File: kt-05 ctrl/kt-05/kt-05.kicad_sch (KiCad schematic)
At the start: 14 parts, among them CN1 PJ-332A-6A, CN2 PJ-332A-6A, CN3 Pogo Pin Receptor Right, U1 SLSS49E-3, U2 SLSS49E-3, U6 H11L1S(TA), U7 Pogo Pin Left, U8 AP2112K-3.3

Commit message: core mainboard
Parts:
- removed CN1, CN2: PJ-332A-6A, easyeda2kicad:AUDIO-SMD_PJ-332A-6A, symbol easyeda2kicad:PJ-332A-6A
- removed U1, U2: SLSS49E-3, samparts:SLSS49E_Hall_Switch_MX, symbol easyeda2kicad:SLSS49E-3
- removed U8: AP2112K-3.3, Package_TO_SOT_SMD:SOT-23-5, symbol Regulator_Linear:AP2112K-3.3
- added C1, C2, C4: 10u, Capacitor_SMD:C_0402_1005Metric, symbol Device:C
- added C3: 0.1u, Capacitor_SMD:C_0402_1005Metric, symbol Device:C
- added C5, C6: 1u, Capacitor_SMD:C_0402_1005Metric, symbol Device:C
- added CN10, CN11, CN12, CN13, CN14, CN3, CN5, CN6, CN7, CN8, CN9: YTC1P-6030-01, easyeda2kicad:SMD-1_BD2.0-H10.0, symbol easyeda2kicad:YTC1P-6030-01
- added CN15: MIDI IN, easyeda2kicad:AUDIO-SMD_PJ-327A5JJ, symbol easyeda2kicad:PJ-327A5JJ
- added CN16: MIDI OUT, easyeda2kicad:AUDIO-SMD_PJ-327A5JJ, symbol easyeda2kicad:PJ-327A5JJ
- added D2: SS34_C8678, easyeda2kicad:SMA_L4.3-W2.6-LS5.2-RD, symbol easyeda2kicad:SS34_C8678
- added D3: 1N4148W, Diode_SMD:D_SOD-123, symbol Diode:1N4148W
- added FPC1: 0.5K-A-8PB, easyeda2kicad:FPC-SMD_8P-P0.50_HDGC_0.5K-A-8PB, symbol easyeda2kicad:0.5K-A-8PB
- added H2: WAFER-PH2.0-2PWB, easyeda2kicad:CONN-SMD_2P-P2.00_XUNPU_WAFER-PH2.0-2PWB, symbol easyeda2kicad:WAFER-PH2.0-2PWB
- added H3: MountingHole_Pad, MountingHole:MountingHole_2.7mm_M2.5_DIN965_Pad_TopBottom, symbol Mechanical:MountingHole_Pad
- added J1: Conn_01x06, Connector_PinHeader_2.54mm:PinHeader_1x06_P2.54mm_Vertical, symbol Connector_Generic:Conn_01x06
- added Q1, Q2, Q3: AO3401A, Package_TO_SOT_SMD:SOT-23, symbol Transistor_FET:AO3401A
- added R2, R24, R6, R7, R8, R9: 10K, Resistor_SMD:R_0402_1005Metric, symbol Device:R
- added R20: 5.1k, Resistor_SMD:R_0402_1005Metric, symbol Device:R
- added R21, R22, R23: 100K, Resistor_SMD:R_0402_1005Metric, symbol Device:R
- added R25: 1M, Resistor_SMD:R_0402_1005Metric, symbol Device:R
- added R26: 10, Resistor_SMD:R_0402_1005Metric, symbol Device:R
- added R27: 33, Resistor_SMD:R_0402_1005Metric, symbol Device:R
- added R28, R29: 470, Resistor_SMD:R_0402_1005Metric, symbol Device:R
- added R5: 22R, Resistor_SMD:R_0402_1005Metric, symbol Device:R
- added SW1: ESP RST, easyeda2kicad:SW-SMD_L3.9-W3.0-P4.45, symbol easyeda2kicad:TS-1088-AR02016
- added SW2: ESP BOOT, easyeda2kicad:SW-SMD_L3.9-W3.0-P4.45, symbol easyeda2kicad:TS-1088-AR02016
- added U1: SK6812MINI-HS, easyeda2kicad:LED-SMD_4P-L3.5-W3.5-BR_SK6812MINI-HS, symbol easyeda2kicad:SK6812MINI-HS
- added U10, U11, U12, U13, U14, U15, U16, U17, U18, U19, U20, U21, U22, U23, U7: H3V3U10B, easyeda2kicad:DFN1006-2L-BI, symbol easyeda2kicad:H3V3U10B
- added U2: AP2112K-3.3, Package_TO_SOT_SMD:SOT-23-5, symbol Regulator_Linear:AP2112K-3.3
- added U3: MCP73831-2-OT, Package_TO_SOT_SMD:SOT-23-5, symbol Battery_Management:MCP73831-2-OT
- added U4: PS-5850SVB-6PL, easyeda2kicad:SW-SMD_6P-L5.8-W5.8-P2.00-LS11.3, symbol easyeda2kicad:PS-5850SVB-6PL
- added U6: ATtiny1616-M, Package_DFN_QFN:VQFN-20-1EP_3x3mm_P0.4mm_EP1.7x1.7mm, symbol MCU_Microchip_ATtiny:ATtiny1616-M
- added U8: ESP32-S3-MINI-1, RF_Module:ESP32-S2-MINI-1, symbol RF_Module:ESP32-S3-MINI-1
- renumbered CN3 to CN4, D2 to D1, F2 to F1, R5 to R3, U6 to U5, U7 to U9
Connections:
- net +3.3V: now also R4.1, U5.6 (VCC), C2.1, C3.1, FPC1.7, J1.2 (Pin_2), R24.1, R27.1, R28.2, R5.2, R6.1, R7.1, R8.1, R9.1, U1.3 (VDD), U2.5 (VOUT), U6.4 (VCC), U8.3 (3V3)
- net +5V: now also R2.2, R20.1, U3.4 (V_{DD}), U4.3
- net DN: now also U8.23 (USB_D-)
- net DP: now also U8.24 (USB_D+)
- net GND: now also U5.5 (GND), C1.2, C2.2, C3.2, C4.2, C5.2, C6.2, CN16.1, CN16.2, FPC1.10, FPC1.2, FPC1.9, H2.2, H2.3, H2.4, J1.1 (Pin_1), R21.2, R25.2, SW1.2, SW2.2, U1.1 (GND), U10.2, U11.2, U12.2, U13.2, U14.1, U15.1, U16.1, U17.1, U18.1, U19.1, U2.2 (GND), U20.1, U21.1, U22.1, U23.1, U3.2 (V_{SS}), U6.21 (GND), U6.3 (GND), U7.1, U8.1 (GND), U8.2 (GND), U8.42 (GND), U8.43 (GND), U8.46 (GND), U8.47 (GND), U8.48 (GND), U8.49 (GND), U8.50 (GND), U8.51 (GND), U8.52 (GND), U8.53 (GND), U8.54 (GND), U8.55 (GND), U8.56 (GND), U8.57 (GND), U8.58 (GND), U8.59 (GND), U8.60 (GND), U8.61 (GND), U8.62 (GND), U8.63 (GND), U8.64 (GND), U8.65 (GND)
- net SCL0: now also J1.5 (Pin_5), R6.2, U11.1, U6.14 (PB0), U8.5 (IO1)
- net SCL1: now also R8.2, U13.1, U8.38 (IO42)
- net SDA0: now also J1.4 (Pin_4), R7.2, U10.1, U6.13 (PB1), U8.6 (IO2)
- net SDA1: now also R9.2, U12.1, U8.37 (IO41)
- net at U5.1 (AN): now also D3.1 (K), R29.1
- net at U5.2 (CAT): now also CN15.4, D3.2 (A)
- net ESP_RXD0: now reaches U5.4 (VO)
- net ESP_RXD0: now also R28.1, U8.40 (RXD0)
- removed net VBUS: CN4.3, R4.2, U9.2
- new net: CN16.4, R26.2
- new net: D2.2 (A), Q3.1 (G), R21.1, U4.2
- new net: FPC1.1, R5.1
- new net: R20.2, U3.5 (PROG)
- new net: CN15.3, R29.2
- new net: R2.1, U2.3 (EN)
- new net: CN16.3, R27.2
- new net A0: CN6.1, U15.2, U6.5 (PA4)
- new net A1: CN14.1, U23.2, U6.6 (PA5)
- new net A14: CN9.1, U18.2, U6.20 (PA1)
- new net A15: CN8.1, U17.2, U6.1 (PA2)
- new net A16: CN7.1, U16.2, U6.2 (PA3)
- new net A2: CN13.1, U22.2, U6.7 (PA6)
- new net A3: CN12.1, U21.2, U6.8 (PA7)
- new net A4: U6.9 (PB5)
- new net CG_STAT: U3.1 (STAT), U8.36 (IO40)
- new net D10: CN3.1, U6.15 (PC0), U7.2
- new net D11: CN5.1, U14.2, U6.16 (PC1)
- new net D12: CN11.1, U20.2, U6.17 (PC2)
- new net D13: CN10.1, U19.2, U6.18 (PC3)
- new net DBLTAP: C6.1, R25.1, U8.29 (IO34)
- new net ESP_BOOT: SW2.1, U8.4 (IO0)
- new net ESP_RST: C5.1, R24.2, SW1.1, U8.45 (EN)
- new net ESP_TXD0: R26.1, U8.39 (TXD0)
- new net NEO: U1.2 (DIN), U8.15 (IO11)
- new net TFT_CS: FPC1.8, U8.22 (IO18)
- new net TFT_DC: FPC1.4, U8.19 (IO15)
- new net TFT_MOSI: FPC1.5, U8.20 (IO16)
- new net TFT_RST: FPC1.3, U8.18 (IO14)
- new net TFT_SCK: FPC1.6, U8.21 (IO17)
- new net TXD: J1.6 (Pin_6), U6.12 (PB2)
- new net UPDI: J1.3 (Pin_3), R4.2, U6.19 (~{RESET}/PA0)
- new net VBAT: C4.1, H2.1, Q3.3 (D), U3.3 (V_{BAT})
- new net VHIGH: C1.1, D2.1 (K), Q1.2 (S), Q2.2 (S), Q3.2 (S), R22.1, R23.1, U2.1 (VIN)
- new net VLEFT: Q1.3 (D), U9.2
- new net VLEFTCTL: Q1.1 (G), R23.2, U8.7 (IO3)
- new net VRIGHT: CN4.3, Q2.3 (D)
- new net VRIGHTCTL: Q2.1 (G), R22.2, U8.35 (IO39)
- no-connect marks 2 -> 15
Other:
- note added: "1.14in screen https://www.buydisplay.com/1-14-inch-tft-lcd-display-ips-panel-screen-135x240-for-smart-watch"
- note added: "Battery 420mAh https://www.pkcell.com/product/lp552535-420mah-3-7v/"
- note added: "UPDI/debug header"
- moved on the sheet: CN4, D1, F1, R1, R3, U5, U9, USBC1

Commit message: ch
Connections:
- net GND: now also CN4.1, U9.4; no longer CN4.4, U9.1
- net SCL0: now also U9.1; no longer U9.4
- net SCL1: now also CN4.4; no longer CN4.1
- net SDA0: now also U9.2; no longer U9.3
- net SDA1: now also CN4.3; no longer CN4.2
- net VLEFT: now also U9.3; no longer U9.2
- net VRIGHT: now also CN4.2; no longer CN4.3
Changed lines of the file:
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@@
 		(lib_id "easyeda2kicad:YZ165615055F-04025-01")
 		(at 532.13 102.87 0)
+		(mirror x)
 		(unit 1)
 		(exclude_from_sim no)
@@
 		(on_board yes)
 		(dnp no)
-		(fields_autoplaced yes)
 		(property "Reference" "U9"
-			(at 535.94 101.5999 0)
+			(at 535.94 104.1401 0)
 			(effects
 				(font
@@
 		)
 		(property "Value" "Pogo Pin Left"
-			(at 535.94 104.1399 0)
+			(at 535.94 101.6001 0)
 			(effects
 				(font
@@
 		)
 		(property "Footprint" "easyeda2kicad:CONN-SMD_4P-L11.0-W5.5-P2.50_YZ165615055F-04025-01"
-			(at 532.13 114.3 0)
+			(at 532.13 91.44 0)
 			(effects
 				(font
@@
 		)
 		(property "LCSC Part" "C5296819"
-			(at 532.13 116.84 0)
+			(at 532.13 88.9 0)
 			(effects
 				(font
@@
 		(lib_id "easyeda2kicad:YZ199315035T-04025-01")
 		(at 532.13 116.84 0)
+		(mirror x)
 		(unit 1)
 		(exclude_from_sim no)
@@
 		(on_board yes)
 		(dnp no)
-		(fields_autoplaced yes)
 		(property "Reference" "CN4"
-			(at 535.94 115.5699 0)
+			(at 535.94 118.1101 0)
 			(effects
 				(font
@@
 		)
 		(property "Value" "Pogo Pin Receptor Right"
-			(at 535.94 118.1099 0)
+			(at 535.94 115.5701 0)
 			(effects
 				(font
@@
 		)
 		(property "Footprint" "easyeda2kicad:CONN-SMD_YZ199315035T-04025-01"
-			(at 532.13 128.27 0)
+			(at 532.13 105.41 0)
 			(effects
 				(font
@@
 		)
 		(property "LCSC Part" "C5296825"
-			(at 532.13 130.81 0)
+			(at 532.13 102.87 0)
 			(effects
 				(font

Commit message: many
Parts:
- added R10, R11: 10K, Resistor_SMD:R_0402_1005Metric, symbol Device:R
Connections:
- net GND: now also R10.2
- net VBAT: now also R11.1
- net BAT_DET: now reaches U8.17 (IO13)
- net BAT_DET: now also R10.1, R11.2

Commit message: prod
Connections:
- net A14: now also U6.14 (PB0); no longer U6.20 (PA1)
- net A15: now also U6.13 (PB1); no longer U6.1 (PA2)
- net A16: now also U6.10 (PB4); no longer U6.2 (PA3)
- net SCL0: now also U6.1 (PA2); no longer U6.14 (PB0)
- net SDA0: now also U6.20 (PA1); no longer U6.13 (PB1)
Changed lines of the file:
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@@
 	)
 	(no_connect
+		(at 215.9 38.1)
+	)
+	(no_connect
 		(at 43.18 175.26)
 	)
@@
 	)
 	(no_connect
-		(at 215.9 63.5)
-	)
-	(no_connect
 		(at 92.71 60.96)
 	)
@@
 	(wire
 		(pts
-			(xy 218.44 33.02) (xy 215.9 33.02)
+			(xy 215.9 33.02) (xy 220.98 33.02)
 		)
 		(stroke
@@
 	(wire
 		(pts
-			(xy 218.44 35.56) (xy 215.9 35.56)
+			(xy 215.9 35.56) (xy 220.98 35.56)
 		)
 		(stroke
@@
 	(wire
 		(pts
+			(xy 228.6 55.88) (xy 215.9 55.88)
+		)
+		(stroke
+			(width 0)
+			(type default)
+		)
+	)
+	(wire
+		(pts
 			(xy 92.71 53.34) (xy 87.63 53.34)
 		)
@@
 	(wire
 		(pts
+			(xy 228.6 53.34) (xy 215.9 53.34)
+		)
+		(stroke
+			(width 0)
+			(type default)
+		)
+	)
+	(wire
+		(pts
 			(xy 118.11 114.3) (xy 104.14 114.3)
 		)
@@
 	(wire
 		(pts
-			(xy 218.44 38.1) (xy 215.9 38.1)
-		)
-		(stroke
-			(width 0)
-			(type default)
-		)
-	)
-	(wire
-		(pts
 			(xy 200.66 71.12) (xy 200.66 73.66)
 		)
@@
 	(wire
 		(pts
-			(xy 218.44 53.34) (xy 215.9 53.34)
-		)
-		(stroke
-			(width 0)
-			(type default)
-		)
-	)
-	(wire
-		(pts
 			(xy 257.81 64.77) (xy 260.35 64.77)
 		)
@@
 	(wire
 		(pts
+			(xy 215.9 63.5) (xy 228.6 63.5)
+		)
+		(stroke
+			(width 0)
+			(type default)
+		)
+	)
+	(wire
+		(pts
 			(xy 34.29 60.96) (xy 34.29 58.42)
 		)
@@
 	(wire
 		(pts
-			(xy 218.44 55.88) (xy 215.9 55.88)
-		)
-		(stroke
-			(width 0)
-			(type default)
-		)
-	)
-	(wire
-		(pts
 			(xy 218.44 58.42) (xy 215.9 58.42)
 		)
@@
 		)
 	)
-	(global_label "A16"
-		(shape input)
-		(at 218.44 38.1 0)
-		(fields_autoplaced yes)
-		(effects
-			(font
-				(size 1.27 1.27)
-			)
-			(justify left)
-		)
-		(property "Intersheetrefs" "${INTERSHEET_REFS}"
-			(at 224.9328 38.1 0)
-			(effects
-				(font
-					(size 1.27 1.27)
-				)
-				(justify left)
-				(hide yes)
-			)
-		)
-	)
-	(global_label "SCL0"
-		(shape bidirectional)
-		(at 218.44 53.34 0)
-		(fields_autoplaced yes)
-		(effects
-			(font
-				(size 1.27 1.27)
-			)
-			(justify left)
-		)
-		(property "Intersheetrefs" "${INTERSHEET_REFS}"
-			(at 227.2536 53.34 0)
-			(effects
-				(font
-					(size 1.27 1.27)
-				)
-				(justify left)
-				(hide yes)
-			)
-		)
-	)
 	(global_label "TFT_CS"
 		(shape input)
@@
 		)
 	)
+	(global_label "A16"
+		(shape input)
+		(at 237.49 38.1 0)
+		(fields_autoplaced yes)
+		(effects
+			(font
+				(size 1.27 1.27)
+			)
+			(justify left)
+		)
+		(property "Intersheetrefs" "${INTERSHEET_REFS}"
+			(at 243.9828 38.1 0)
+			(effects
+				(font
+					(size 1.27 1.27)
+				)
+				(justify left)
+				(hide yes)
+			)
+		)
+	)
 	(global_label "DN"
 		(shape input)
@@
 	(global_label "A15"
 		(shape input)
-		(at 218.44 35.56 0)
+		(at 237.49 35.56 0)
 		(fields_autoplaced yes)
 		(effects
@@
 		)
 		(property "Intersheetrefs" "${INTERSHEET_REFS}"
-			(at 224.9328 35.56 0)
+			(at 243.9828 35.56 0)
 			(effects
 				(font
@@
 		)
 	)
+	(global_label "A16"
+		(shape input)
+		(at 228.6 63.5 0)
+		(fields_autoplaced yes)
+		(effects
+			(font
+				(size 1.27 1.27)
+			)
+			(justify left)
+		)
+		(property "Intersheetrefs" "${INTERSHEET_REFS}"
+			(at 235.0928 63.5 0)
+			(effects
+				(font
+					(size 1.27 1.27)
+				)
+				(justify left)
+				(hide yes)
+			)
+		)
+	)
 	(global_label "BAT_DET"
 		(shape input)
@@
 		)
 	)
+	(global_label "A15"
+		(shape input)
+		(at 228.6 55.88 0)
+		(fields_autoplaced yes)
+		(effects
+			(font
+				(size 1.27 1.27)
+			)
+			(justify left)
+		)
+		(property "Intersheetrefs" "${INTERSHEET_REFS}"
+			(at 235.0928 55.88 0)
+			(effects
+				(font
+					(size 1.27 1.27)
+				)
+				(justify left)
+				(hide yes)
+			)
+		)
+	)
 	(global_label "DP_PRE"
 		(shape input)
@@
 		)
 	)
+	(global_label "A14"
+		(shape input)
+		(at 228.6 53.34 0)
+		(fields_autoplaced yes)
+		(effects
+			(font
+				(size 1.27 1.27)
+			)
+			(justify left)
+		)
+		(property "Intersheetrefs" "${INTERSHEET_REFS}"
+			(at 235.0928 53.34 0)
+			(effects
+				(font
+					(size 1.27 1.27)
+				)
+				(justify left)
+				(hide yes)
+			)
+		)
+	)
 	(global_label "SDA0"
 		(shape bidirectional)
@@
 		)
 	)
-	(global_label "A14"
-		(shape input)
-		(at 218.44 33.02 0)
-		(fields_autoplaced yes)
-		(effects
-			(font
-				(size 1.27 1.27)
-			)
-			(justify left)
-		)
-		(property "Intersheetrefs" "${INTERSHEET_REFS}"
-			(at 224.9328 33.02 0)
-			(effects
-				(font
-					(size 1.27 1.27)
-				)
-				(justify left)
-				(hide yes)
-			)
-		)
-	)
 	(global_label "D12"
 		(shape input)
@@
 		)
 	)
+	(global_label "SCL0"
+		(shape bidirectional)
+		(at 220.98 35.56 0)
+		(fields_autoplaced yes)
+		(effects
+			(font
+				(size 1.27 1.27)
+			)
+			(justify left)
+		)
+		(property "Intersheetrefs" "${INTERSHEET_REFS}"
+			(at 229.7936 35.56 0)
+			(effects
+				(font
+					(size 1.27 1.27)
+				)
+				(justify left)
+				(hide yes)
+			)
+		)
+	)
 	(global_label "DN_PRE"
 		(shape input)
@@
 		)
 	)
+	(global_label "SDA0"
+		(shape bidirectional)
+		(at 220.98 33.02 0)
+		(fields_autoplaced yes)
+		(effects
+			(font
+				(size 1.27 1.27)
+			)
+			(justify left)
+		)
+		(property "Intersheetrefs" "${INTERSHEET_REFS}"
+			(at 229.8541 33.02 0)
+			(effects
+				(font
+					(size 1.27 1.27)
+				)
+				(justify left)
+				(hide yes)
+			)
+		)
+	)
 	(global_label "ESP_RXD0"
 		(shape bidirectional)
@@
 		)
 	)
+	(global_label "A14"
+		(shape input)
+		(at 237.49 33.02 0)
+		(fields_autoplaced yes)
+		(effects
+			(font
+				(size 1.27 1.27)
+			)
+			(justify left)
+		)
+		(property "Intersheetrefs" "${INTERSHEET_REFS}"
+			(at 243.9828 33.02 0)
+			(effects
+				(font
+					(size 1.27 1.27)
+				)
+				(justify left)
+				(hide yes)
+			)
+		)
+	)
 	(global_label "ESP_RST"
 		(shape input)
@@
 			(effects
 				(font
-					(size 1.27 1.27)
-				)
-				(justify left)
-				(hide yes)
-			)
-		)
-	)
-	(global_label "SDA0"
-		(shape bidirectional)
-		(at 218.44 55.88 0)
-		(fields_autoplaced yes)
-		(effects
-			(font
-				(size 1.27 1.27)
-			)
-			(justify left)
-		)
-		(property "Intersheetrefs" "${INTERSHEET_REFS}"
-			(at 227.3141 55.88 0)
-			(effects
-				(font

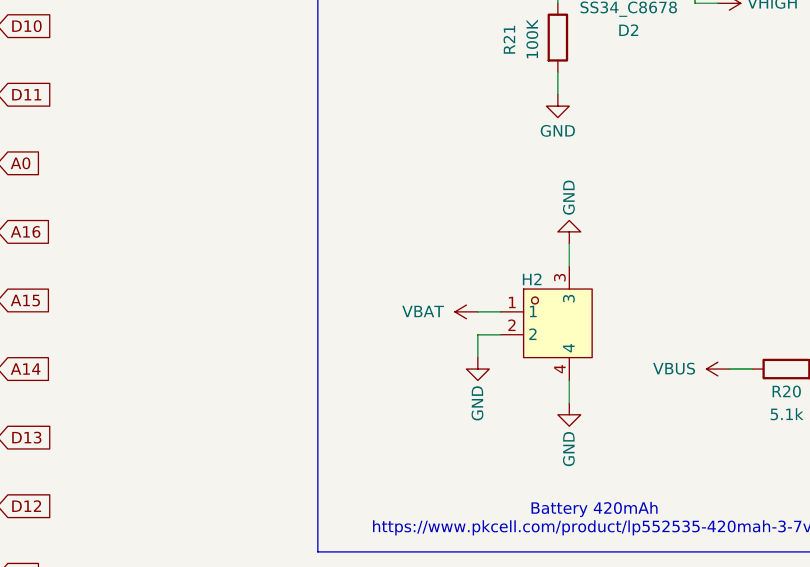
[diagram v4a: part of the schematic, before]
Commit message: improved fuses
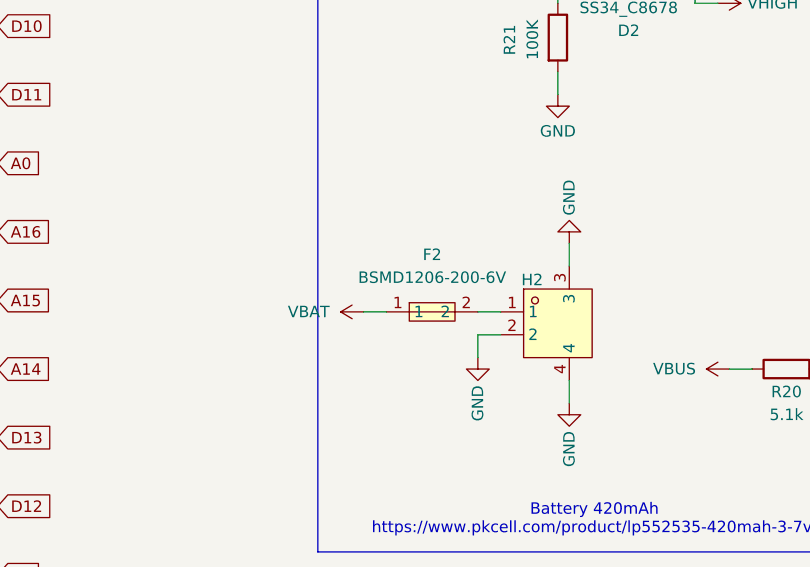
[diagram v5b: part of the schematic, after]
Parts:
- added F2: BSMD1206-200-6V, easyeda2kicad:F1206, symbol easyeda2kicad:BSMD1206-200-6V
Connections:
- net VBAT: now also F2.1; no longer H2.1
- new net: F2.2, H2.1
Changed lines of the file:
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@@
 	(wire
 		(pts
-			(xy 320.04 118.11) (xy 317.5 118.11)
-		)
-		(stroke
-			(width 0)
-			(type default)
-		)
-	)
-	(wire
-		(pts
 			(xy 444.5 19.05) (xy 447.04 19.05)
 		)
@@
 	(wire
 		(pts
+			(xy 307.34 118.11) (xy 304.8 118.11)
+		)
+		(stroke
+			(width 0)
+			(type default)
+		)
+	)
+	(wire
+		(pts
 			(xy 328.93 27.94) (xy 331.47 27.94)
 		)
@@
 	(wire
 		(pts
+			(xy 317.5 118.11) (xy 320.04 118.11)
+		)
+		(stroke
+			(width 0)
+			(type default)
+		)
+	)
+	(wire
+		(pts
 			(xy 111.76 161.29) (xy 111.76 163.83)
 		)
@@
 	)
 	(symbol
+		(lib_id "easyeda2kicad:BSMD1206-200-6V")
+		(at 312.42 118.11 0)
+		(unit 1)
+		(exclude_from_sim no)
+		(in_bom yes)
+		(on_board yes)
+		(dnp no)
+		(fields_autoplaced yes)
+		(property "Reference" "F2"
+			(at 312.42 111.76 0)
+			(effects
+				(font
+					(size 1.27 1.27)
+				)
+			)
+		)
+		(property "Value" "BSMD1206-200-6V"
+			(at 312.42 114.3 0)
+			(effects
+				(font
+					(size 1.27 1.27)
+				)
+			)
+		)
+		(property "Footprint" "easyeda2kicad:F1206"
+			(at 312.42 125.73 0)
+			(effects
+				(font
+					(size 1.27 1.27)
+				)
+				(hide yes)
+			)
+		)
+		(property "Datasheet" "https://lcsc.com/product-detail/PTC-Resettable-Fuses_BHFUSE-BSMD1206-200-6V_C883134.html"
+			(at 312.42 128.27 0)
+			(effects
+				(font
+					(size 1.27 1.27)
+				)
+				(hide yes)
+			)
+		)
+		(property "Description" ""
+			(at 312.42 118.11 0)
+			(effects
+				(font
+					(size 1.27 1.27)
+				)
+				(hide yes)
+			)
+		)
+		(property "LCSC Part" "C883134"
+			(at 312.42 130.81 0)
+			(effects
+				(font
+					(size 1.27 1.27)
+				)
+				(hide yes)
+			)
+		)
+		(pin "1"
+		)
+		(pin "2"
+		)
+		(instances
+			(project "kt-05"
+				(path "/aa5e2b95-c80c-4ceb-b804-b3a5918dc7d7"
+					(reference "F2")
+					(unit 1)
+				)
+			)
+		)
+	)
+	(symbol
 		(lib_id "easyeda2kicad:H3V3U10B")
 		(at 224.79 147.32 0)
@@
 	(symbol
 		(lib_id "power:VBUS")
-		(at 317.5 118.11 90)
+		(at 304.8 118.11 90)
 		(unit 1)
 		(exclude_from_sim no)
@@
 		(dnp no)
 		(property "Reference" "#PWR053"
-			(at 321.31 118.11 0)
+			(at 308.61 118.11 0)
 			(effects
 				(font
@@
 		)
 		(property "Value" "VBAT"
-			(at 311.404 118.11 90)
+			(at 298.704 118.11 90)
 			(effects
 				(font
@@
 		)
 		(property "Footprint" ""
-			(at 317.5 118.11 0)
+			(at 304.8 118.11 0)
 			(effects
 				(font
@@
 		)
 		(property "Datasheet" ""
-			(at 317.5 118.11 0)
+			(at 304.8 118.11 0)
 			(effects
 				(font
@@
 		)
 		(property "Description" "Power symbol creates a global label with name \"VBUS\""
-			(at 317.5 118.11 0)
+			(at 304.8 118.11 0)
 			(effects
 				(font

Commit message: production 1
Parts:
- added C7: 1u, Capacitor_SMD:C_0402_1005Metric, symbol Device:C
- added C8, C9: 10u, Capacitor_SMD:C_0402_1005Metric, symbol Device:C
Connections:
- net +3.3V: now also C7.1, C8.1, C9.1
- net GND: now also C7.2, C8.2, C9.2
